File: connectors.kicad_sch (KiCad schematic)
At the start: 2 parts

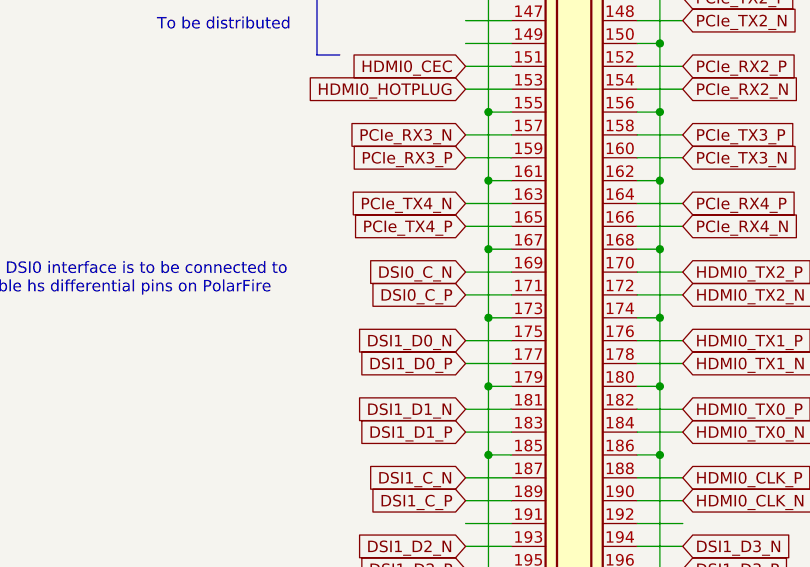
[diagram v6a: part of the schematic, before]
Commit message: [#53847] Add 2-lane CSI transceiver resistor array
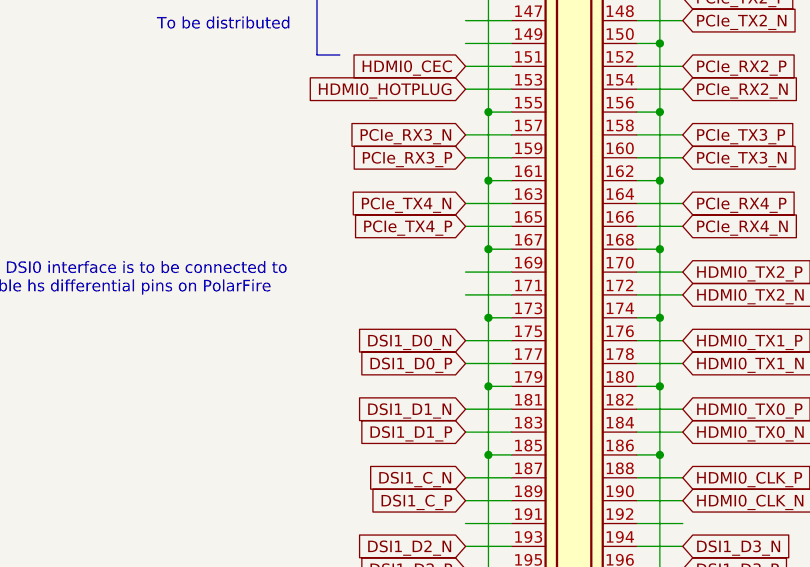
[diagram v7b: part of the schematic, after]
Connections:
- net DSI0_C_N: no longer names the net of J?.169
- net DSI0_C_P: no longer names the net of J?.171
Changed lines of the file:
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@@
-    )
-  )
-  (global_label "DSI0_C_P" (shape input) (at 306.07 170.18 180) (fields_autoplaced)
-    (effects (font (size 1.27 1.27)) (justify right))
-    (property "Intersheet References" "${INTERSHEET_REFS}" (id 0) (at 294.8879 170.1006 0)
-      (effects (font (size 1.27 1.27)) (justify right) hide)
     )
   )
@@
     )
   )
-  (global_label "DSI0_C_N" (shape input) (at 306.07 167.64 180) (fields_autoplaced)
-    (effects (font (size 1.27 1.27)) (justify right))
-    (property "Intersheet References" "${INTERSHEET_REFS}" (id 0) (at 294.8274 167.5606 0)
-      (effects (font (size 1.27 1.27)) (justify right) hide)
-    )
-  )

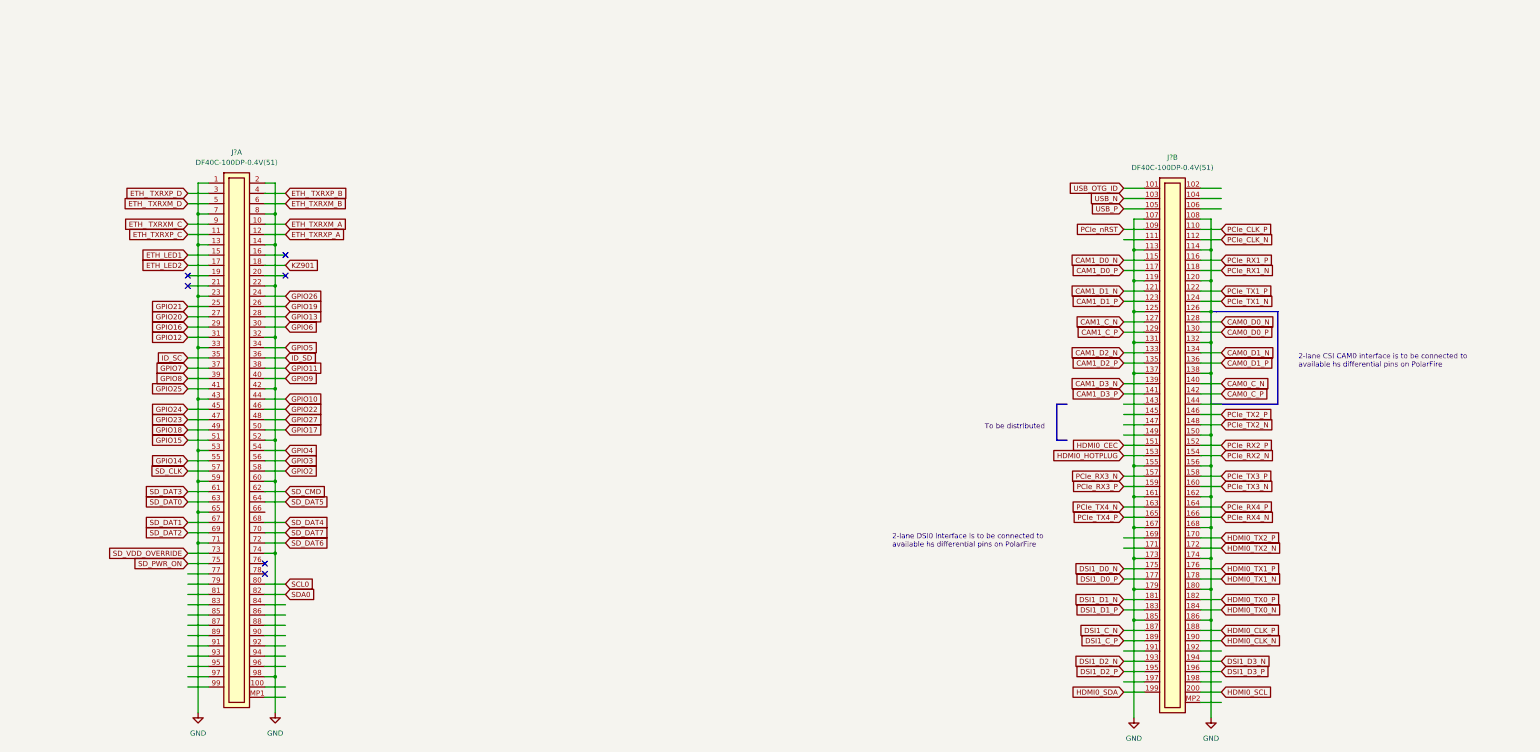
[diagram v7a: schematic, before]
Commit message: [#53979] Add 2-lane CSI transceiver resistor array
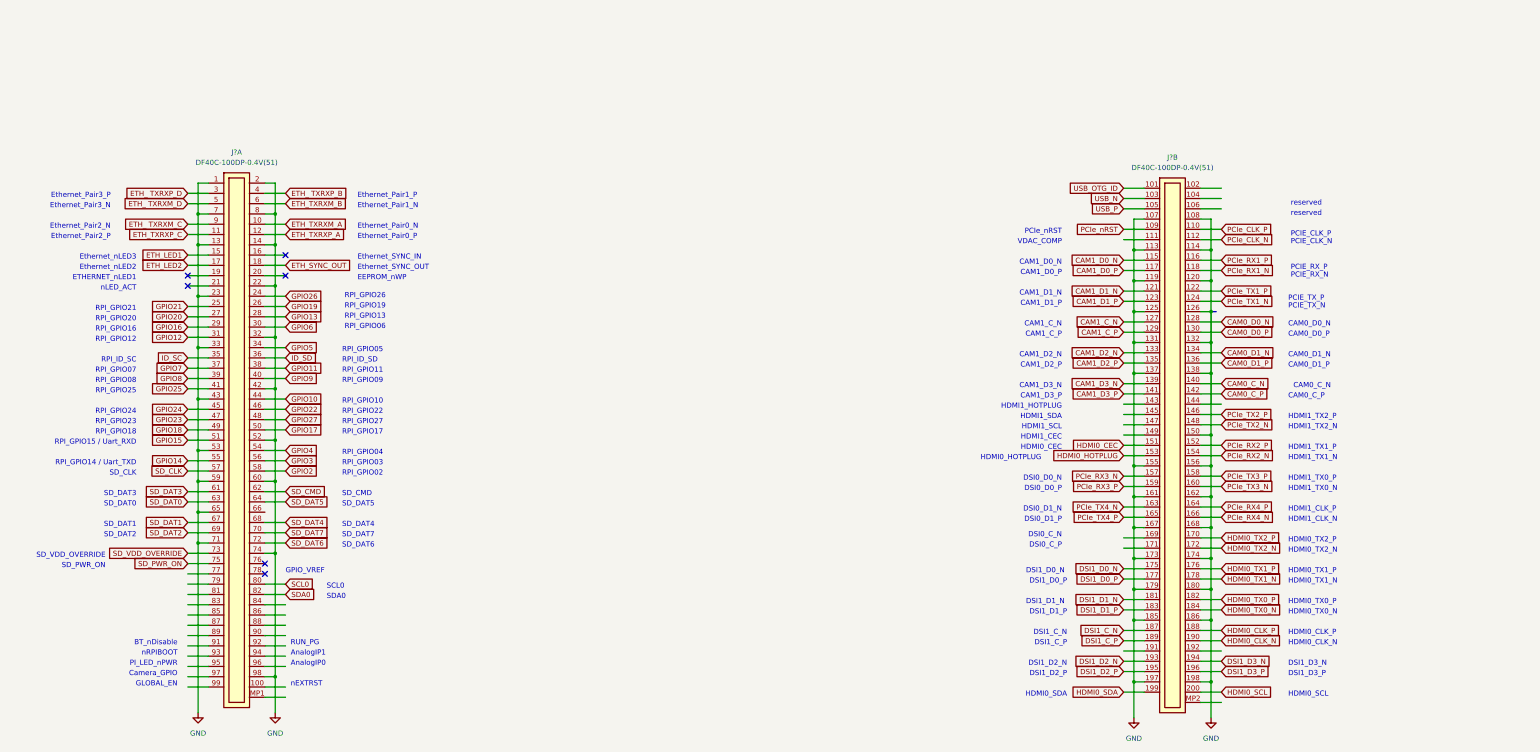
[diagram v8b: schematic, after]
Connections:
- net GND: now also J?.197, J?.198
- net KZ901 renamed ETH_SYNC_OUT
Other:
- note added: "AnalogIP0"
- note added: "AnalogIP1"
- note added: "BT_nDisable"
- note added: "CAM0_C_N"
- note added: "CAM0_C_P"
- note added: "CAM0_D0_N"
- note added: "CAM0_D0_P"
- note added: "CAM0_D1_N"
- note added: "CAM0_D1_P"
- note added: "CAM1_C_N"
- note added: "CAM1_C_P"
- note added: "CAM1_D0_N"
- note added: "CAM1_D0_P"
- note added: "CAM1_D1_N"
- note added: "CAM1_D1_P"
- note added: "CAM1_D2_N"
- note added: "CAM1_D2_P"
- note added: "CAM1_D3_N"
- note added: "CAM1_D3_P"
- note added: "Camera_GPIO"
- note added: "DSI0_C_N"
- note added: "DSI0_C_P"
- note added: "DSI0_D0_N"
- note added: "DSI0_D0_P"
- note added: "DSI0_D1_N"
- note added: "DSI0_D1_P"
- note added: "DSI1_C_N"
- note added: "DSI1_C_P"
- note added: "DSI1_D0_N"
- note added: "DSI1_D0_P"
- note added: "DSI1_D1_N"
- note added: "DSI1_D1_P"
- note added: "DSI1_D2_N"
- note added: "DSI1_D2_P"
- note added: "DSI1_D3_N"
- note added: "DSI1_D3_P"
- note added: "EEPROM_nWP"
- note added: "ETHERNET_nLED1"
- note added: "Ethernet_Pair0_N"
- note added: "Ethernet_Pair0_P"
- note added: "Ethernet_Pair1_N"
- note added: "Ethernet_Pair1_P"
- note added: "Ethernet_Pair2_N"
- note added: "Ethernet_Pair2_P"
- note added: "Ethernet_Pair3_N"
- note added: "Ethernet_Pair3_P"
- note added: "Ethernet_SYNC_IN"
- note added: "Ethernet_SYNC_OUT"
- note added: "Ethernet_nLED2"
- note added: "Ethernet_nLED3"
- note added: "GLOBAL_EN"
- note added: "GPIO_VREF"
- note added: "HDMI0_CEC"
- note added: "HDMI0_CLK_N"
- note added: "HDMI0_CLK_P"
- note added: "HDMI0_HOTPLUG"
- note added: "HDMI0_SCL"
- note added: "HDMI0_SDA"
- note added: "HDMI0_TX0_N"
- note added: "HDMI0_TX0_P"
- note added: "HDMI0_TX1_N"
- note added: "HDMI0_TX1_P"
- note added: "HDMI0_TX2_N"
- note added: "HDMI0_TX2_P"
- note added: "HDMI1_CEC"
- note added: "HDMI1_CLK_N"
- note added: "HDMI1_CLK_P"
- note added: "HDMI1_HOTPLUG"
- note added: "HDMI1_SCL"
- note added: "HDMI1_SDA"
- note added: "HDMI1_TX0_N"
- note added: "HDMI1_TX0_P"
- note added: "HDMI1_TX1_N"
- note added: "HDMI1_TX1_P"
- note added: "HDMI1_TX2_N"
- note added: "HDMI1_TX2_P"
- note added: "PCIE_CLK_N"
- note added: "PCIE_CLK_P"
- note added: "PCIE_RX_N"
- note added: "PCIE_RX_P"
- note added: "PCIE_TX_N"
- note added: "PCIE_TX_P"
- note added: "PCIe_nRST"
- note added: "PI_LED_nPWR"
- note added: "RPI_GPIO02"
- note added: "RPI_GPIO03"
- note added: "RPI_GPIO04"
- note added: "RPI_GPIO05"
- note added: "RPI_GPIO06"
- note added: "RPI_GPIO07"
- note added: "RPI_GPIO08"
- note added: "RPI_GPIO09"
- note added: "RPI_GPIO10"
- note added: "RPI_GPIO11"
- note added: "RPI_GPIO12"
- note added: "RPI_GPIO13"
- note added: "RPI_GPIO14 / Uart_TXD"
- note added: "RPI_GPIO15 / Uart_RXD"
- note added: "RPI_GPIO16"
- note added: "RPI_GPIO17"
- note added: "RPI_GPIO18"
- note added: "RPI_GPIO19"
- note added: "RPI_GPIO20"
- note added: "RPI_GPIO21"
- note added: "RPI_GPIO22"
- note added: "RPI_GPIO23"
- note added: "RPI_GPIO24"
- note added: "RPI_GPIO25"
- note added: "RPI_GPIO26"
- note added: "RPI_GPIO27"
- note added: "RPI_ID_SC"
- note added: "RPI_ID_SD"
- note added: "RUN_PG"
- note added: "SCL0"
- note added: "SDA0"
- note added: "SD_CLK"
- note added: "SD_CMD"
- note added: "SD_DAT0"
- note added: "SD_DAT1"
- note added: "SD_DAT2"
- note added: "SD_DAT3"
- note added: "SD_DAT4"
- note added: "SD_DAT5"
- note added: "SD_DAT6"
- note added: "SD_DAT7"
- note added: "SD_PWR_ON"
- note added: "SD_VDD_OVERRIDE"
- note added: "VDAC_COMP"
- note added: "nEXTRST"
- note added: "nLED_ACT"
- note added: "nRPIBOOT"
- note added: "reserved"
- note removed: "2-lane CSI CAM0 interface is to be connected to available hs differential pins on PolarFire"
- note removed: "2-lane DSI0 interface is to be connected to available hs differential pins on PolarFire"
- note removed: "To be distributed"
